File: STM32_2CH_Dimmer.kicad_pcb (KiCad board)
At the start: 2 copper layers, 56 x 55.4 mm, 38 parts, among them J1 Power, J2 Encoder1, J3 Encoder2, J4 LED1, J5 LED2, Q1 IRF3708, Q2 IRF3708, SW1 Config, U1 173950378, U2 DS18B20, U3 STM32F103Generic, U4 AT24CS32, U5 CC1101

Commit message: update
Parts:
- C7: footprint Capacitor_SMD:C_0603_1608Metric_Pad1.05x0.95mm_HandSolder -> Capacitor_SMD:C_0805_2012Metric_Pad1.15x1.40mm_HandSolder
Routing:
- net GND: track 8.91 -> 13.4 mm

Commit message: some fixes
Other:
- board text added: "= solder Pin"
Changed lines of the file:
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@@
   (general
     (thickness 1.6)
-    (drawings 57)
+    (drawings 59)
     (tracks 268)
     (zones 0)
@@
     )
   )
+  (gr_text "= solder Pin" (at 153.25 113.25 270) (layer B.SilkS)
+    (effects (font (size 1 1) (thickness 0.15)) (justify mirror))
+  )
+  (gr_circle (center 153.274754 120) (end 154.124754 120.95) (layer B.SilkS) (width 0.15))
   (gr_text V1.0 (at 170.25 95.5 270) (layer B.SilkS)
     (effects (font (size 1 1) (thickness 0.15)) (justify mirror))

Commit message: V1.1
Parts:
- added C1: 10µ, Capacitor_SMD:C_1210_3225Metric_Pad1.42x2.65mm_HandSolder, F.Cu at (190.2, 110.5)
- C2: renamed from C5; value 10µ -> 22µ
- C8: renamed from C6; footprint Capacitor_SMD:C_0603_1608Metric_Pad1.05x0.95mm_HandSolder -> Capacitor_SMD:C_0805_2012Metric_Pad1.15x1.40mm_HandSolder
- U1: value 173950378 -> LC78
- renumbered C7 to C3, C1 to C4, C3 to C5, C2 to C6, C4 to C7, J4 to J2, J2 to J3, J3 to J4, R5 to R1, R9 to R10, R6 to R2, R7 to R3, R1 to R4, R2 to R5, R8 to R6, R10 to R7, R3 to R8, R4 to R9, U3 to U2, U5 to U3, U2 to U5
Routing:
- net +24V: track 57.9 -> 65.1 mm
- net GND: vias 0 -> 61
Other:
- board text added: "V1.1"
- board text removed: "V1.0"

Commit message: V1.2
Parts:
- U1: value LC78 -> LC78_03-05
- moved U1 6.02 mm to (183.3, 117.9), turned to 90 degrees
- moved REF** 0.89 mm to (147.9, 70.6)
- moved REF** 0.80 mm to (147.8, 121.0)
- moved REF** 0.64 mm to (199.0, 120.9)
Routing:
- net +24V: track 65.1 -> 62.7 mm
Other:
- board text added: "V1.2"
- board text removed: "V1.1"

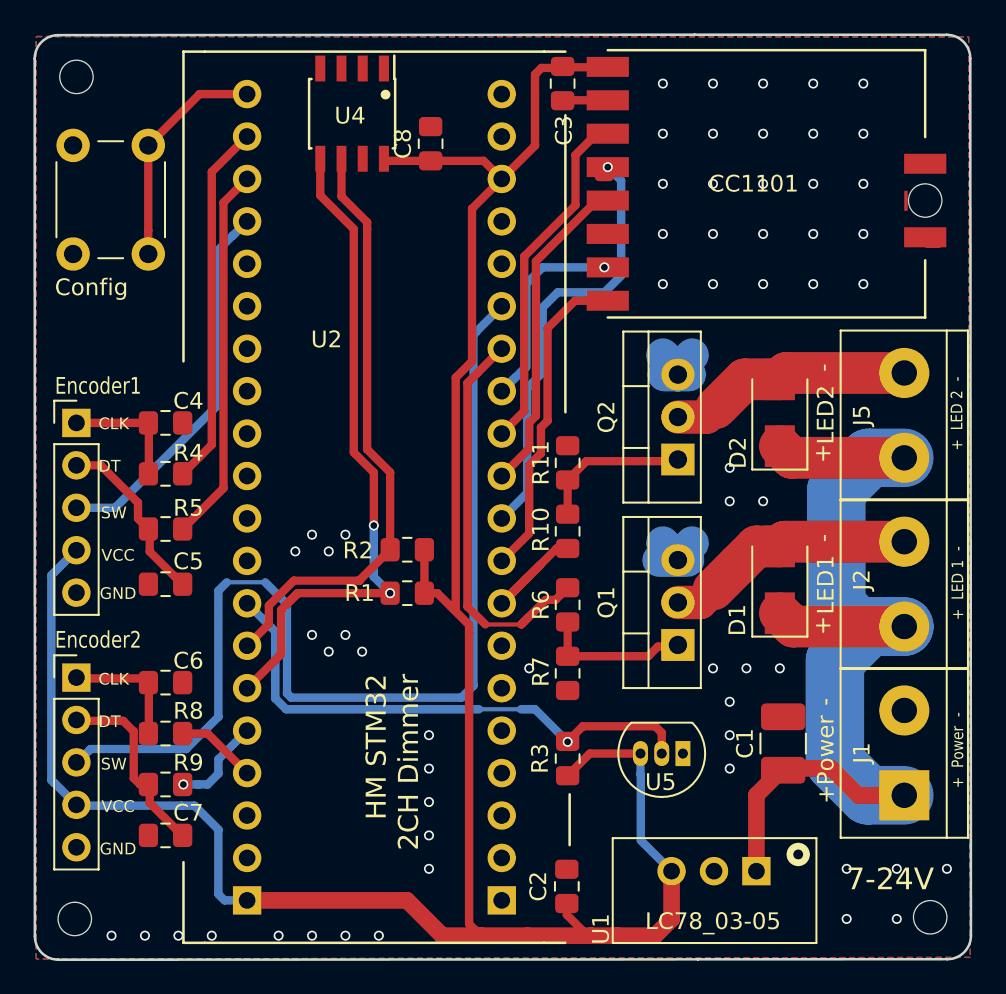
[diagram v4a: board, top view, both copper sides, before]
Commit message: V1.3
minor fixes
add test pads for serial connection
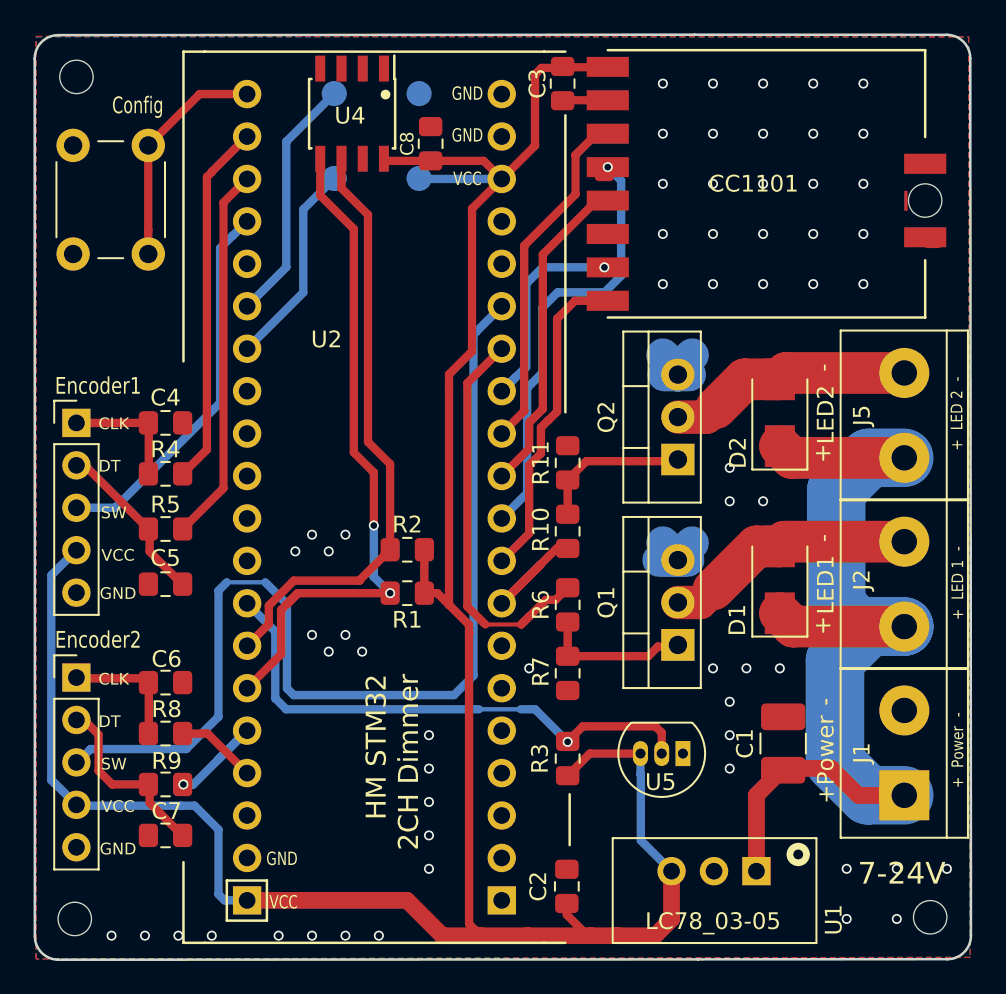
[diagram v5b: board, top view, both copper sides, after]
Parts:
- added TP1: TestPoint, TestPoint:TestPoint_Pad_D1.5mm, B.Cu at (168.4, 76.7)
- added TP2: TestPoint, TestPoint:TestPoint_Pad_D1.5mm, B.Cu at (163.3, 76.7)
- added TP3: TestPoint, TestPoint:TestPoint_Pad_D1.5mm, B.Cu at (163.3, 71.6)
- added TP4: TestPoint, TestPoint:TestPoint_Pad_D1.5mm, B.Cu at (168.4, 71.6)
- U1: footprint Homebrew:WE_FDSM_173950378 -> Homebrew:LC78_03-05
- moved G*** 0.99 mm to (165.3, 96.4)
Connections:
- U2 pad 14: Net-(U2-Pad14) -> /RX
- U2 pad 15: Net-(U2-Pad15) -> /TX
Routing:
- net /TX: track 0.00 -> 14.9 mm
- net /RX: track 0.00 -> 12.3 mm
- net VCC: track 147.9 -> 152.8 mm
- net /DT2: track 5.70 -> 7.57 mm
- net /SW2: track 62.4 -> 61.7 mm
- net Net-(C5-Pad1): track 10.6 -> 10.00 mm
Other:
- board text added: "RX"
- board text added: "Serial"
- board text added: "TX"
- board text added: "V1.3"
- board text removed: "V1.2"

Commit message: update 1.4 final
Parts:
- removed C1: 10µ, Capacitor_SMD:C_1210_3225Metric_Pad1.42x2.65mm_HandSolder
- moved U1 1.96 mm to (182.8, 116.0)
- moved U5 0.62 mm to (184.3, 110.5)
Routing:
- net VCC: track 152.8 -> 158.7 mm
- net +24V: track 62.7 -> 59.5 mm
- net /1WIRE: track 32.6 -> 35.6 mm, vias 1 -> 0
- net GND: vias 61 -> 55
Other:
- board text added: "3.3"
- board text added: "A10"
- board text added: "A3"
- board text added: "A4"
- board text added: "A5"
- board text added: "A6"
- board text added: "A7"
- board text added: "A9"
- board text added: "B0"
- board text added: "B1"
- board text added: "B10"
- board text added: "B12"
- board text added: "B13"
- board text added: "B14"
- board text added: "B15"
- board text added: "B5"
- board text added: "B6"
- board text added: "B7"
- board text added: "B8"
- board text added: "B9"
- board text added: "G"
- board text added: "USB"
- board text added: "V1.4"
- board text removed: "V1.3"

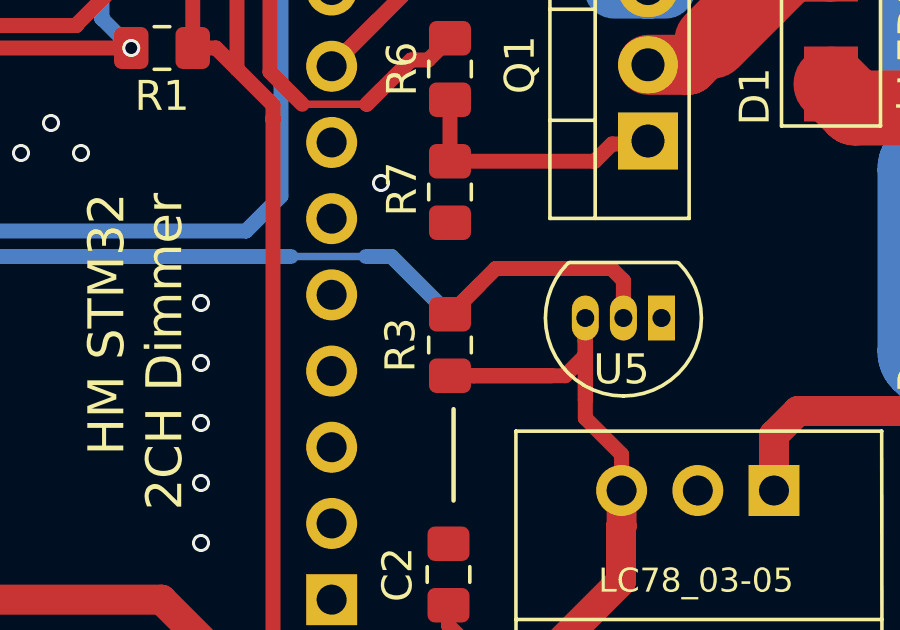
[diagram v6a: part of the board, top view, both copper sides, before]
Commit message: Update V1.5
add missing Via at R3
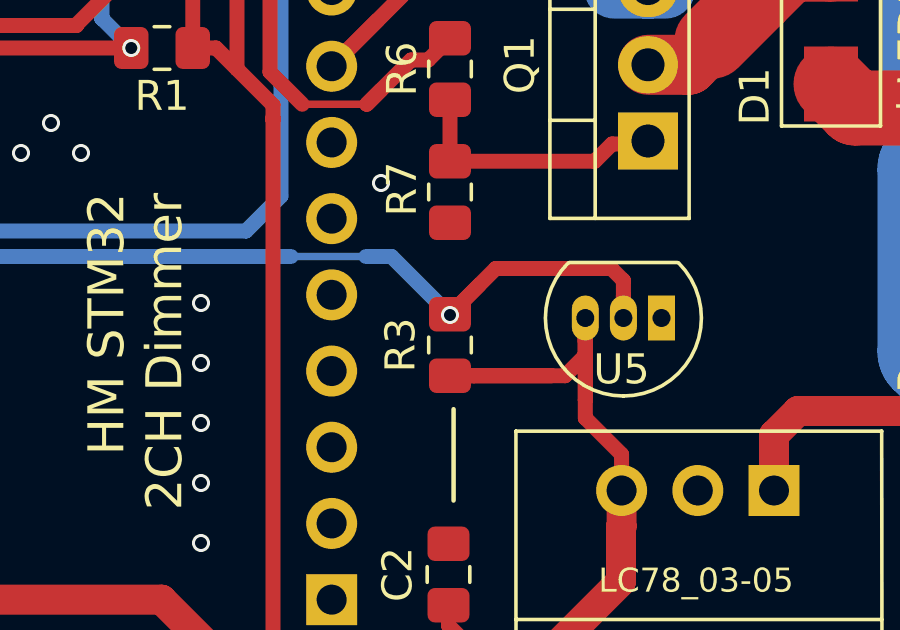
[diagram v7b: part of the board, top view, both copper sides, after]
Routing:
- net /1WIRE: vias 0 -> 1
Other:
- board text added: "V1.5"
- board text removed: "V1.4"
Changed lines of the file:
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@@
-(kicad_pcb (version 20171130) (host pcbnew "(5.1.2)-2")
+(kicad_pcb (version 20171130) (host pcbnew "(5.1.4)-1")
   (general
     (thickness 1.6)
     (drawings 105)
-    (tracks 340)
+    (tracks 342)
     (zones 0)
     (modules 42)
@@
   )
   (gr_circle (center 151.198754 120) (end 152.048754 120.95) (layer B.SilkS) (width 0.15))
-  (gr_text V1.4 (at 181.5 96.3 270) (layer B.SilkS)
+  (gr_text V1.5 (at 181.5 96.3 270) (layer B.SilkS)
     (effects (font (size 1 1) (thickness 0.15)) (justify mirror))
   )
@@
   (segment (start 178.825 108.85) (end 182.68 108.85) (width 0.5) (layer F.Cu) (net 18))
   (segment (start 177.3 110.375) (end 178.825 108.85) (width 0.5) (layer F.Cu) (net 18))
+  (segment (start 177.3 110.4) (end 177.3 110.4) (width 0.5) (layer B.Cu) (net 18))
+  (via (at 177.3 110.4) (size 0.6) (drill 0.4) (layers F.Cu B.Cu) (net 18))
   (segment (start 173.355 86.868) (end 171.8945 88.3285) (width 0.5) (layer F.Cu) (net 19))
   (segment (start 174.525 103.375) (end 172.375 103.375) (width 0.25) (layer F.Cu) (net 19))
